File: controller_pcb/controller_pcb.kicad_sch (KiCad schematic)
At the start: 22 parts, among them IC1 AMS1117-5.0, J1 A_08-LC-TT, J2 SM03B-GHS-TB_LF__SN_, Q1 SI2301CDS-T1-GE3.

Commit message: 3D models added
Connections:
- net GND: now also J2.1, LED1.1 (K)
- net at IC1.2 (VOUT), J1.5, J1.8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: now also R6.2
- net at R6.1: now also LED1.2 (A)
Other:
- moved on the sheet: LED1, R6
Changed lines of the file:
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@@
 		(color 0 0 0 0)
 	)
+	(junction
+		(at 59.69 31.75)
+		(diameter 0)
+		(color 0 0 0 0)
+	)
 	(wire
 		(pts
@@
 	(wire
 		(pts
+			(xy 59.69 31.75) (xy 59.69 39.37)
+		)
+		(stroke
+			(width 0)
+			(type default)
+		)
+	)
+	(wire
+		(pts
 			(xy 237.49 68.58) (xy 217.17 68.58)
 		)
@@
 	(wire
 		(pts
+			(xy 39.37 31.75) (xy 41.91 31.75)
+		)
+		(stroke
+			(width 0)
+			(type default)
+		)
+	)
+	(wire
+		(pts
 			(xy 99.06 27.94) (xy 59.69 27.94)
 		)
@@
 	(wire
 		(pts
-			(xy 59.69 27.94) (xy 59.69 39.37)
+			(xy 59.69 27.94) (xy 59.69 31.75)
 		)
 		(stroke
@@
 	)
 	(symbol
+		(lib_id "power:GND")
+		(at 24.13 31.75 270)
+		(unit 1)
+		(exclude_from_sim no)
+		(in_bom yes)
+		(on_board yes)
+		(dnp no)
+		(fields_autoplaced yes)
+		(property "Reference" "#PWR08"
+			(at 17.78 31.75 0)
+			(effects
+				(font
+					(size 1.27 1.27)
+				)
+				(hide yes)
+			)
+		)
+		(property "Value" "GND"
+			(at 20.32 31.7499 90)
+			(effects
+				(font
+					(size 1.27 1.27)
+				)
+				(justify right)
+			)
+		)
+		(property "Footprint" ""
+			(at 24.13 31.75 0)
+			(effects
+				(font
+					(size 1.27 1.27)
+				)
+				(hide yes)
+			)
+		)
+		(property "Datasheet" ""
+			(at 24.13 31.75 0)
+			(effects
+				(font
+					(size 1.27 1.27)
+				)
+				(hide yes)
+			)
+		)
+		(property "Description" "Power symbol creates a global label with name \"GND\" , ground"
+			(at 24.13 31.75 0)
+			(effects
+				(font
+					(size 1.27 1.27)
+				)
+				(hide yes)
+			)
+		)
+		(pin "1"
+		)
+		(instances
+			(project ""
+				(path "/35628871-c2d7-47c8-b610-2ce05008c7f9"
+					(reference "#PWR08")
+					(unit 1)
+				)
+			)
+		)
+	)
+	(symbol
 		(lib_id "Controller_Comp:CL21B106KOQNNNE")
 		(at 187.96 154.94 0)
@@
 	(symbol
 		(lib_id "Controller_Comp:ERJ-6ENF2200V")
-		(at 100.33 143.51 0)
+		(at 41.91 31.75 0)
 		(unit 1)
 		(exclude_from_sim no)
@@
 		(fields_autoplaced yes)
 		(property "Reference" "R6"
-			(at 109.22 137.16 0)
+			(at 50.8 25.4 0)
 			(effects
 				(font
@@
 		)
 		(property "Value" "ERJ-6ENF2200V"
-			(at 109.22 139.7 0)
+			(at 50.8 27.94 0)
 			(effects
 				(font
@@
 		)
 		(property "Footprint" "Controller_Footprints:ERJ6ENF1000V"
-			(at 114.3 239.7 0)
+			(at 55.88 127.94 0)
 			(effects
 				(font
@@
 		)
 		(property "Datasheet" "https://industrial.panasonic.com/cdbs/www-data/pdf/RDA0000/AOA0000C84.pdf"
-			(at 114.3 339.7 0)
+			(at 55.88 227.94 0)
 			(effects
 				(font
@@
 		)
 		(property "Description" "Precision Thick Film Chip Resistor, 0805, 0.125W"
-			(at 101.346 146.558 0)
+			(at 42.926 34.798 0)
 			(effects
 				(font
@@
 		)
 		(property "Height" "0.7"
-			(at 114.3 539.7 0)
+			(at 55.88 427.94 0)
 			(effects
 				(font
@@
 		)
 		(property "Manufacturer_Name" "Panasonic"
-			(at 114.3 639.7 0)
+			(at 55.88 527.94 0)
 			(effects
 				(font
@@
 		)
 		(property "Manufacturer_Part_Number" "ERJ-6ENF2200V"
-			(at 114.3 739.7 0)
+			(at 55.88 627.94 0)
 			(effects
 				(font
@@
 		)
 		(property "Mouser Part Number" "667-ERJ-6ENF2200V"
-			(at 114.3 839.7 0)
+			(at 55.88 727.94 0)
 			(effects
 				(font
@@
 		)
 		(property "Mouser Price/Stock" "https://www.mouser.co.uk/ProductDetail/Panasonic/ERJ-6ENF2200V?qs=50QC8w71jAu9tJGxfTXkOw%3D%3D"
-			(at 114.3 939.7 0)
+			(at 55.88 827.94 0)
 			(effects
 				(font
@@
 		)
 		(property "Arrow Part Number" "ERJ-6ENF2200V"
-			(at 114.3 1039.7 0)
+			(at 55.88 927.94 0)
 			(effects
 				(font
@@
 		)
 		(property "Arrow Price/Stock" "https://www.arrow.com/en/products/erj-6enf2200v/panasonic?region=nac"
-			(at 114.3 1139.7 0)
+			(at 55.88 1027.94 0)
 			(effects
 				(font
@@
 	(symbol
 		(lib_id "Controller_Comp:150080RS75000")
-		(at 130.81 143.51 0)
+		(at 24.13 31.75 0)
 		(unit 1)
 		(exclude_from_sim no)
@@
 		(fields_autoplaced yes)
 		(property "Reference" "LED1"
-			(at 138.43 133.35 0)
+			(at 31.75 21.59 0)
 			(effects
 				(font
@@
 		)
 		(property "Value" "150080RS75000"
-			(at 138.43 135.89 0)
+			(at 31.75 24.13 0)
 			(effects
 				(font
@@
 		)
 		(property "Footprint" "Controller_Footprints:LEDC2012X70N"
-			(at 143.51 237.16 0)
+			(at 36.83 125.4 0)
 			(effects
 				(font
@@
 		)
 		(property "Datasheet" "https://www.we-online.com/components/products/download/Download_3D_150080RS75000+%28rev1%29.pdf"
-			(at 143.51 337.16 0)
+			(at 36.83 225.4 0)
 			(effects
 				(font
@@
 		)
 		(property "Description" "WL-SMCW SMT Mono-Color Chip LED Waterclear 0805, Red Typ.(@20mA): 625nm, 150mcd, 2.0V, 140 AlInGaP"
-			(at 130.81 149.098 0)
+			(at 24.13 37.338 0)
 			(effects
 				(font
@@
 		)
 		(property "Height" "0.7"
-			(at 143.51 537.16 0)
+			(at 36.83 425.4 0)
 			(effects
 				(font
@@
 		)
 		(property "Manufacturer_Name" "Wurth Elektronik"
-			(at 143.51 637.16 0)
+			(at 36.83 525.4 0)
 			(effects
 				(font
@@
 		)
 		(property "Manufacturer_Part_Number" "150080RS75000"
-			(at 143.51 737.16 0)
+			(at 36.83 625.4 0)
 			(effects
 				(font
@@
 		)
 		(property "Mouser Part Number" "710-150080RS75000"
-			(at 143.51 837.16 0)
+			(at 36.83 725.4 0)
 			(effects
 				(font
@@
 		)
 		(property "Mouser Price/Stock" "https://www.mouser.co.uk/ProductDetail/Wurth-Elektronik/150080RS75000?qs=LlUlMxKIyB2jdCo7bnfgew%3D%3D"
-			(at 143.51 937.16 0)
+			(at 36.83 825.4 0)
 			(effects
 				(font
@@
 		)
 		(property "Arrow Part Number" ""
-			(at 143.51 1037.16 0)
+			(at 36.83 925.4 0)
 			(effects
 				(font
@@
 		)
 		(property "Arrow Price/Stock" ""
-			(at 143.51 1137.16 0)
+			(at 36.83 1025.4 0)
 			(effects
 				(font
@@
 					(unit 1)
 				)
+			)
+		)
+	)
+	(symbol
+		(lib_id "power:GND")
+		(at 278.13 25.4 90)
+		(unit 1)
+		(exclude_from_sim no)
+		(in_bom yes)
+		(on_board yes)
+		(dnp no)
+		(fields_autoplaced yes)
+		(property "Reference" "#PWR011"
+			(at 284.48 25.4 0)
+			(effects
+				(font
+					(size 1.27 1.27)
+				)
+				(hide yes)
+			)
+		)
+		(property "Value" "GND"
+			(at 281.94 25.3999 90)
+			(effects
+				(font
+					(size 1.27 1.27)
+				)
+				(justify right)
+			)
+		)
+		(property "Footprint" ""
+			(at 278.13 25.4 0)
+			(effects
+				(font
+					(size 1.27 1.27)
+				)
+				(hide yes)
+			)
+		)
+		(property "Datasheet" ""
+			(at 278.13 25.4 0)
+			(effects
+				(font
+					(size 1.27 1.27)
+				)
+				(hide yes)
+			)
+		)
+		(property "Description" "Power symbol creates a global label with name \"GND\" , ground"
+			(at 278.13 25.4 0)
+			(effects
+				(font
+					(size 1.27 1.27)
+				)
+				(hide yes)
+			)
+		)
+		(pin "1"
+		)
+		(instances
+			(project ""
+				(path "/35628871-c2d7-47c8-b610-2ce05008c7f9"
+					(reference "#PWR011")
+					(unit 1)
+				)

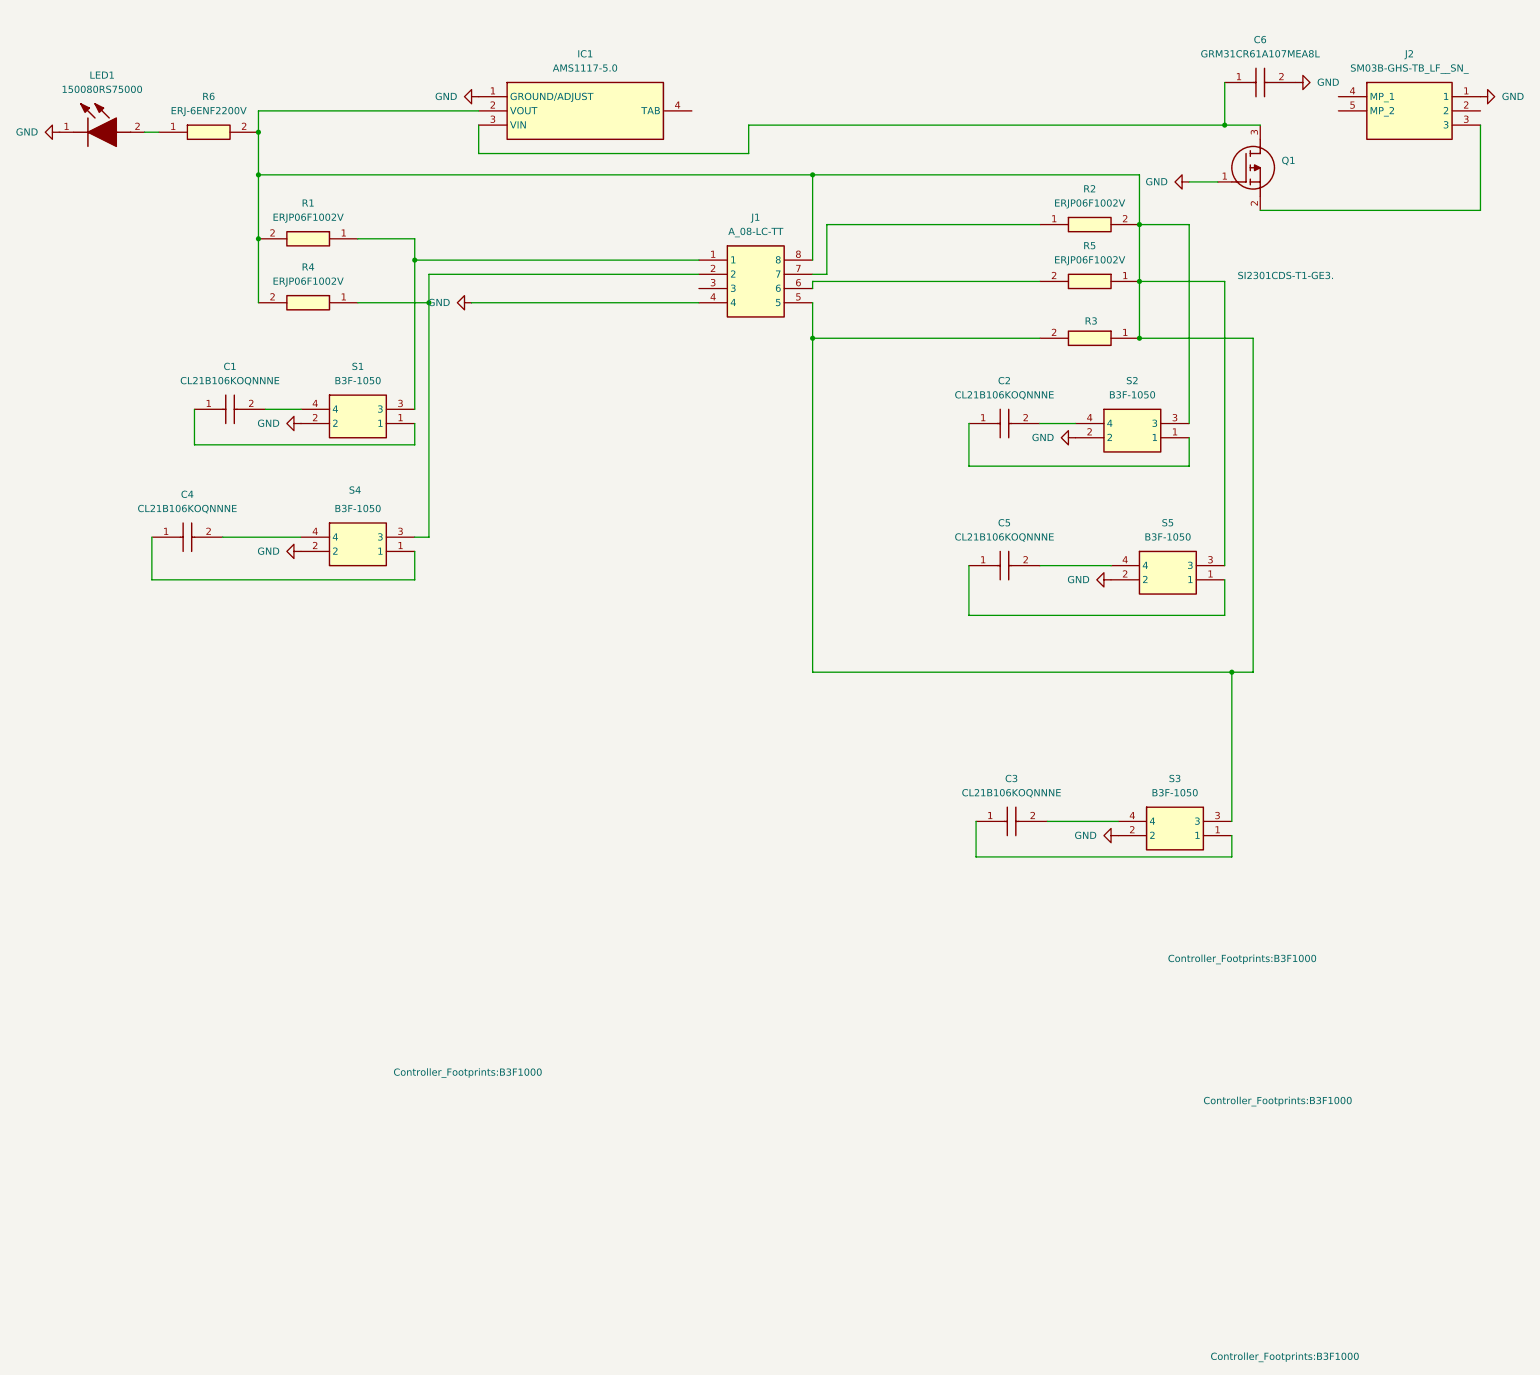
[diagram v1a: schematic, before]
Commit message: Finished routing; added copper plane on front
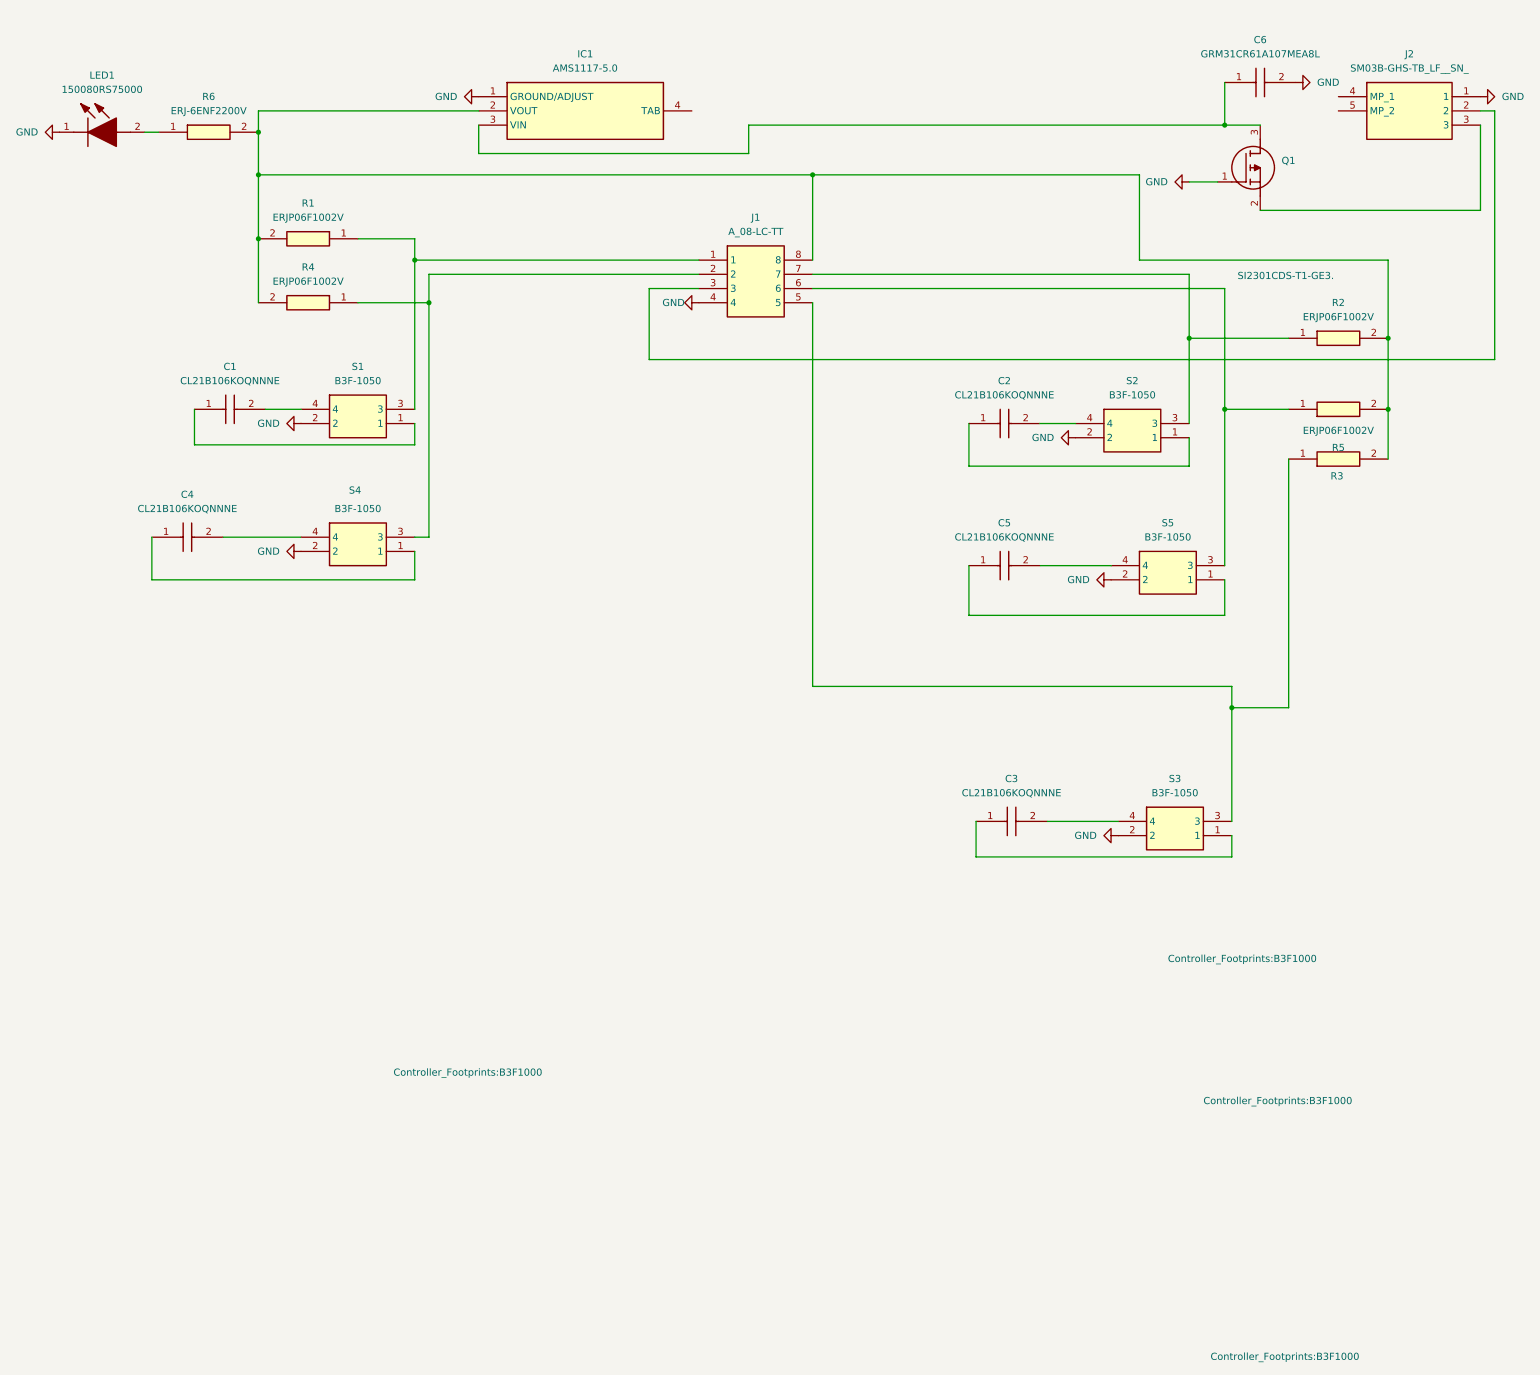
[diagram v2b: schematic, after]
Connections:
- net at J2.2: now also J1.3
- net at IC1.2 (VOUT), J1.8, R1.2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: now also R5.2; no longer J1.5, R3.1, R5.1, S2.3, S3.3, S5.3
- net at J1.7, R2.1: now also S2.3
- net at J1.6: now also R5.1, S5.3; no longer R5.2
- new net: J1.5, R3.1, S3.3
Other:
- moved on the sheet: R2, R3, R5

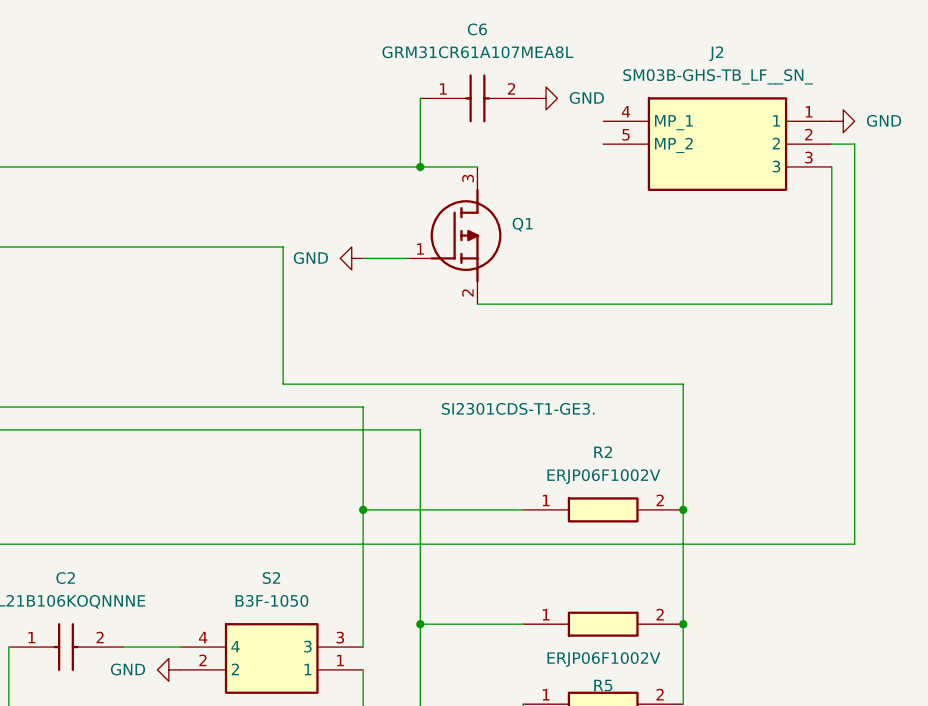
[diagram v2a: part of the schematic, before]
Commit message: Rerouted for button clearance
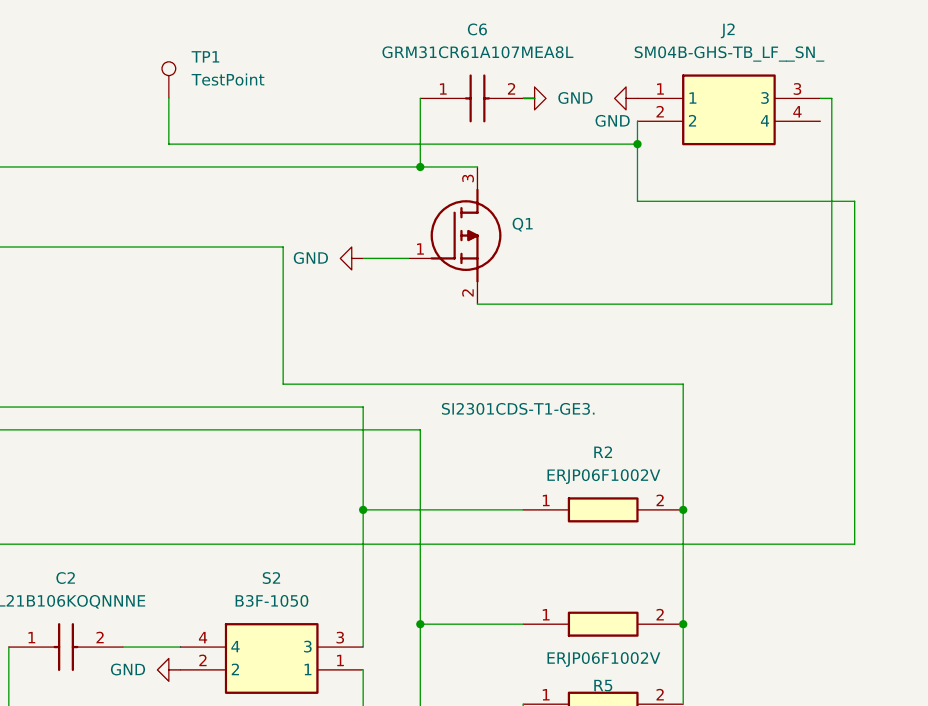
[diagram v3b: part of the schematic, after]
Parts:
- removed J2: SM03B-GHS-TB_LF__SN_, Controller_Footprints:SM03BGHSTBLFSN, symbol Controller_Comp:SM03B-GHS-TB_LF__SN_
- added J2: SM04B-GHS-TB_LF__SN_, SM04B-GHS-TB, symbol Controller_Comp:SM04B-GHS-TB_LF__SN_
- added TP1: TestPoint, TestPoint:TestPoint_Pad_2.0x2.0mm, symbol Connector:TestPoint
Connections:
- net GND: now also J2.1
- net at J1.3: now also J2.2, TP1.1
- net at Q1.2 (S): now also J2.3
